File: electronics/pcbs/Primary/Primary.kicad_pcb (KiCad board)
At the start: 2 copper layers, 102 x 53.3 mm, 27 parts, among them J1 Line Sensor 1, J11 I2C Bus, J12 Battery, J13 Pololu_D24V50F5, J14 Magnet, J2 Line Sensor 2, J3 Line Sensor 3, J4 Line Sensor 4, J5 Line Sensor 5, J6 Line Sensor 6, J7 Servo, J8 Pololu_DRV8834, J9 Stepper Motor, P1 Digital, P10 CONN_01X01, P11 CONN_01X01, P12 CONN_01X01, P13 CONN_01X01, P2 Power, P3 Analog, P4 Analog, P5 PWM, P6 PWM, P7 Communication, P8 CONN_01X01, P9 CONN_01X01

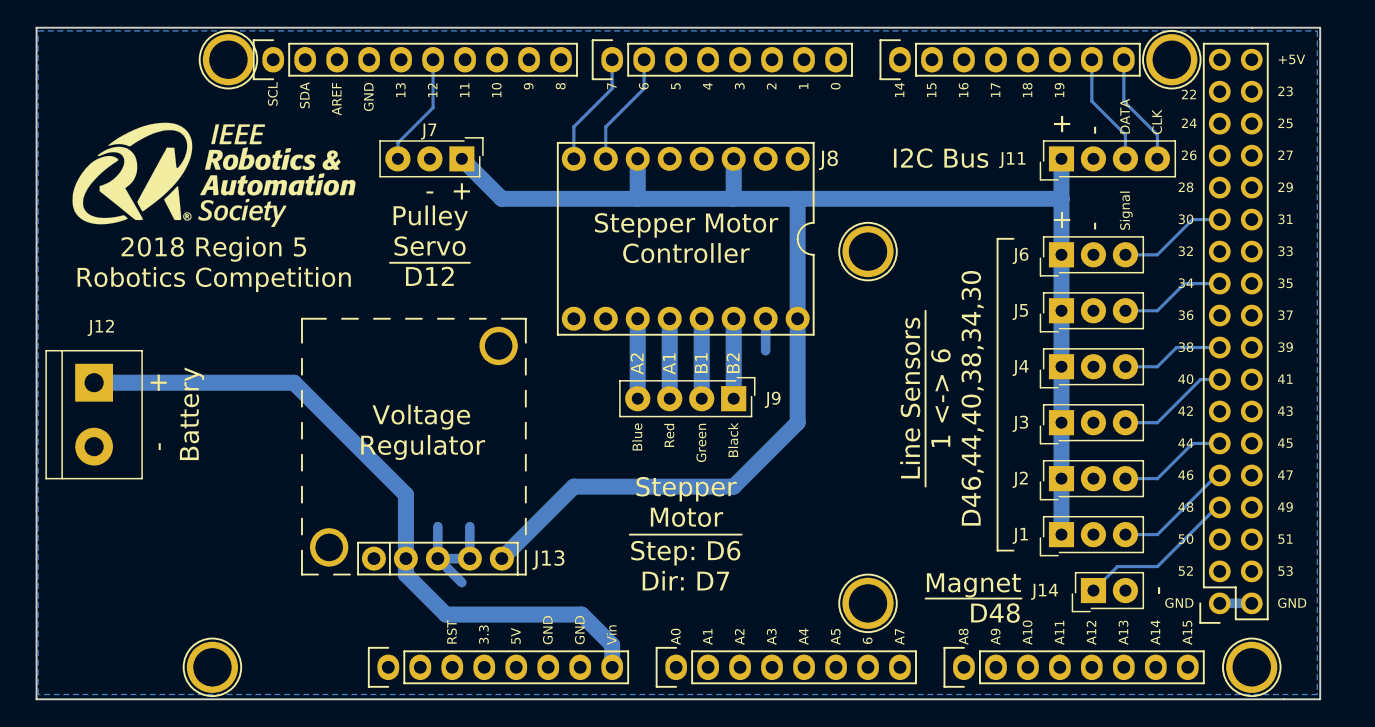
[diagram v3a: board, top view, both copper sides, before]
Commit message: Primary PCB: Modified Primary to be more easily printed with labels on the OtherMill.
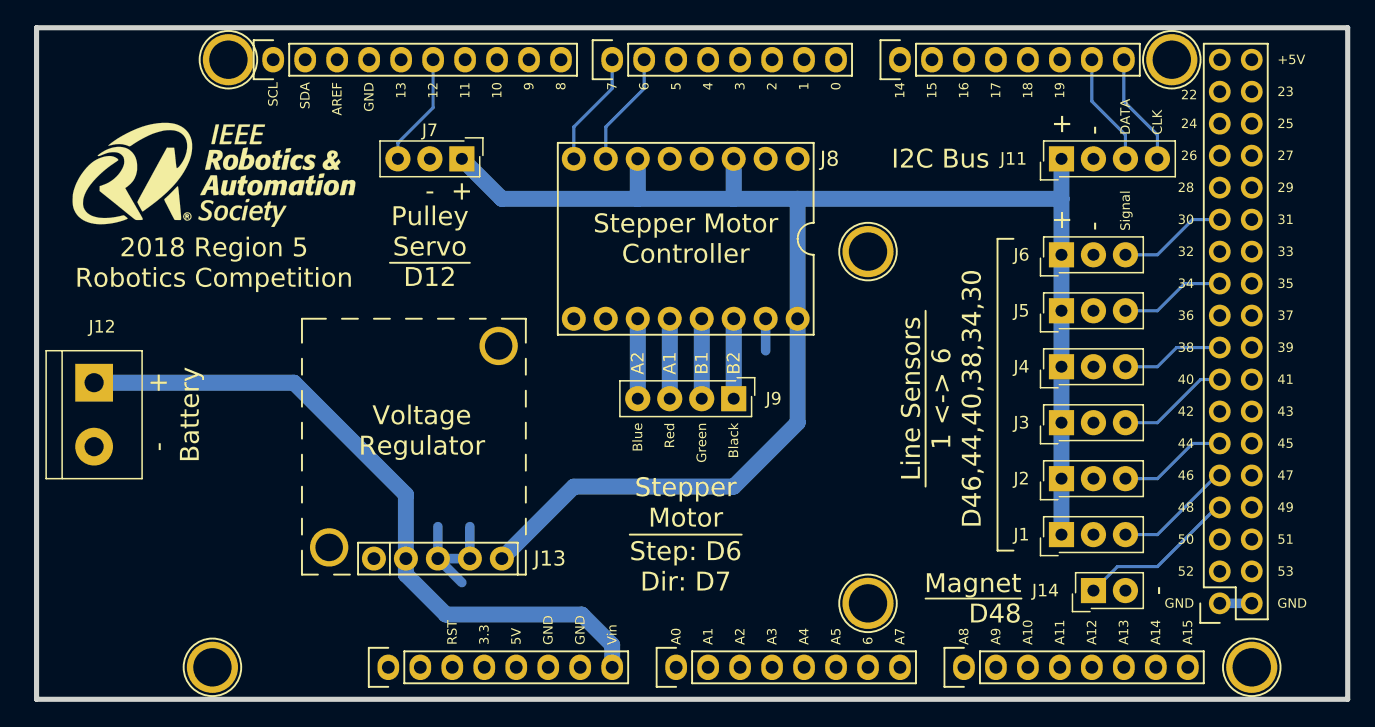
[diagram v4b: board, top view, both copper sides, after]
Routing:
- added copper zone on F.Cu, net GND
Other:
- board size 102 x 53.3 mm -> 104.1 x 53.3 mm
- board text added: "Bk"
- board text added: "Bl"
- board text added: "C"
- board text added: "D"
- board text added: "G"
- board text added: "R"
- board text added: "Sig"
- board text added: "Stepper Motor Step: D6 Dir: D7"

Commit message: Primary PCB: Modified electromagnet circuit to power the magnet with a transistor.
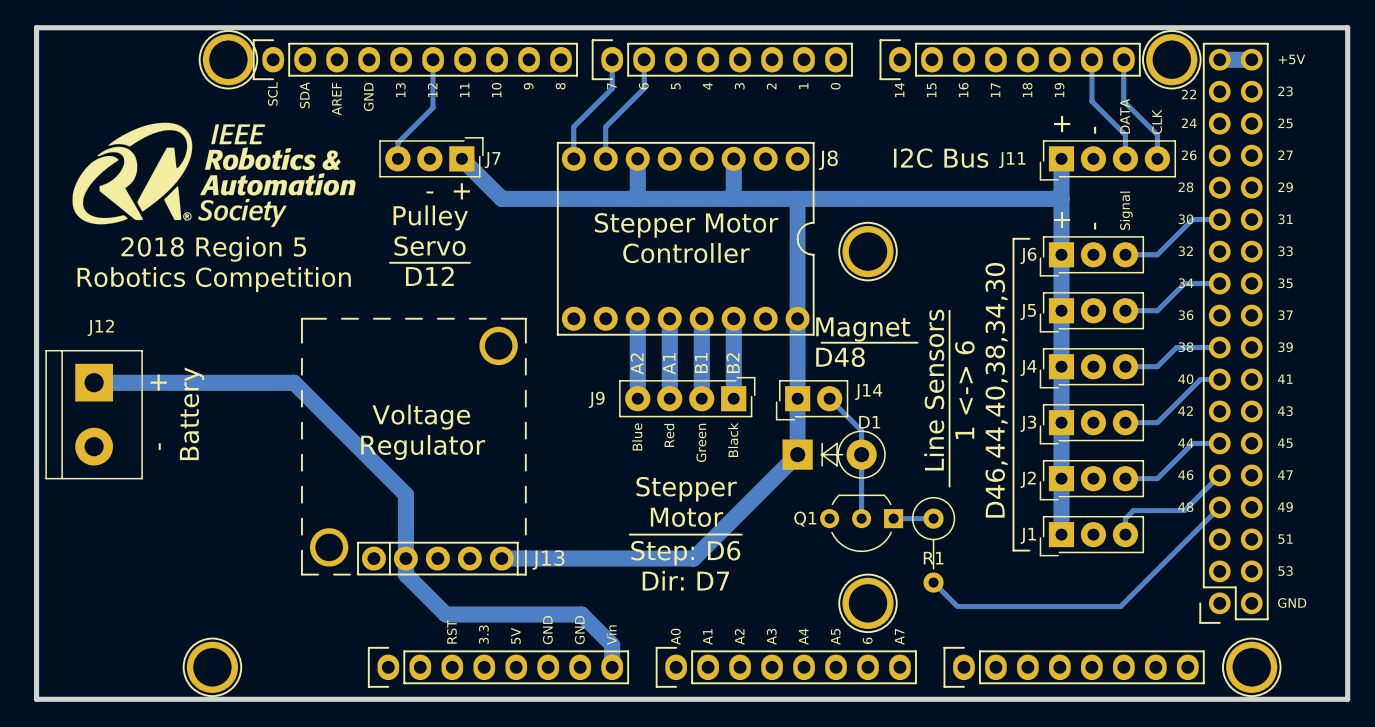
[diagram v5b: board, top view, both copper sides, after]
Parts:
- added D1: D, Diodes_THT:D_DO-15_P5.08mm_Vertical_KathodeUp, F.Cu at (163.8, 102.2)
- added Q1: Q_NPN_BCE, TO_SOT_Packages_THT:TO-92_Inline_Wide, F.Cu at (171.4, 107.3)
- added R1: R, Resistors_THT:R_Axial_DIN0309_L9.0mm_D3.2mm_P5.08mm_Vertical, F.Cu at (174.6, 107.3)
- moved J14 28.0 mm to (163.8, 97.8)
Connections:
- J14 pad 1: /48 -> +5V
- J14 pad 2: GND -> Net-(D1-Pad2)
- P1 pad 35: +5V -> +5VP
- P1 pad 36: +5V -> +5VP
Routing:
- net GND: track 15.4 -> 0.00 mm
- net /48: track 12.8 -> 26.8 mm
- net Net-(D1-Pad2): track 0.00 -> 10.6 mm
- net Net-(Q1-Pad1): track 0.00 -> 3.18 mm
- net +5VP: track 0.00 -> 2.54 mm
- net +5V: track 132.2 -> 133.6 mm
- net /46: track 9.44 -> 10.2 mm
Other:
- net class Default: trace_width 0.25 -> 0.4; via_dia 0.6 -> 0.96; via_drill 0.4 -> 0.64
- net class Ground: clearance 0.2 -> 0.3
- net class HighPower: clearance 0.2 -> 0.3
- board text removed: "50"
- board text removed: "52"
- board text removed: "A10"
- board text removed: "A11"
- board text removed: "A12"
- board text removed: "A13"
- board text removed: "A14"
- board text removed: "A15"
- board text removed: "A8"
- board text removed: "A9"

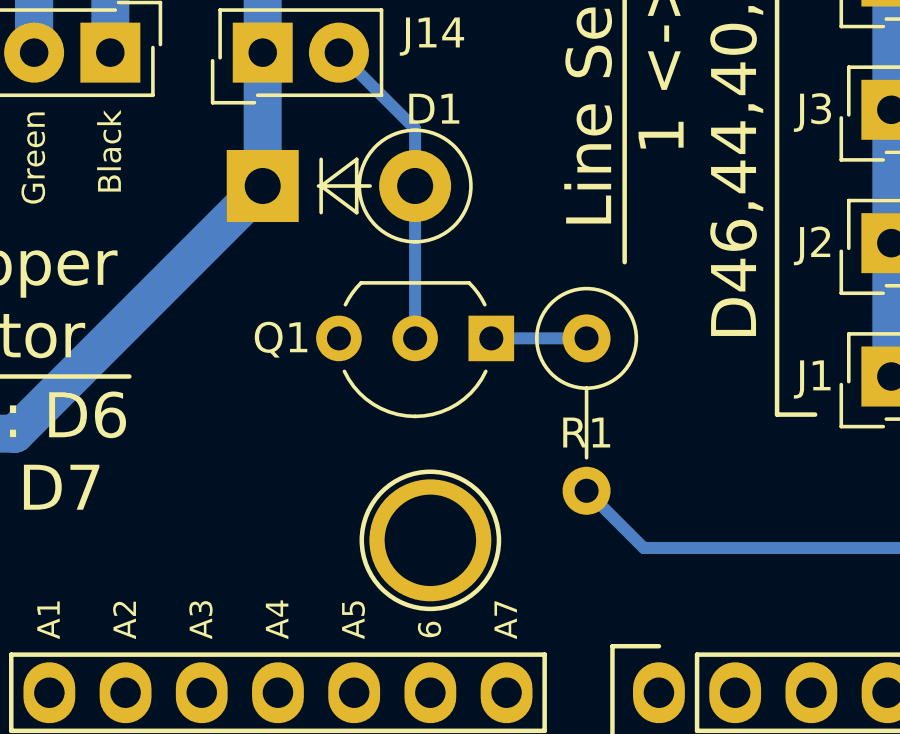
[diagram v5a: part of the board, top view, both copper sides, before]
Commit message: Primary PCB: Corrected transistor pinout and footprint. Gave a value to the resistor attached to the transistor.
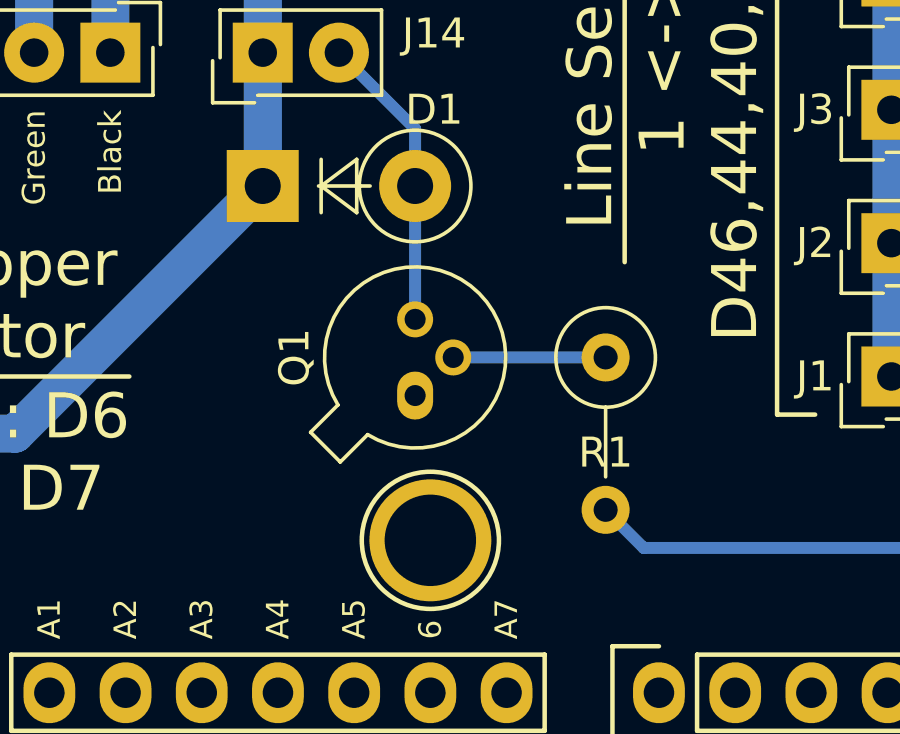
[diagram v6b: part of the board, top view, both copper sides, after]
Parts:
- D1: value D -> 1N914
- Q1: footprint TO_SOT_Packages_THT:TO-92_Inline_Wide -> TO_SOT_Packages_THT:TO-18-3
- R1: value R -> 220
- moved Q1 3.17 mm to (168.9, 109.2), turned to 90 degrees
- moved R1 0.90 mm to (175.3, 108.0)
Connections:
- J13 pad : GND -> (no net)
- Q1 pad 1: Net-(Q1-Pad1) -> GND
- Q1 pad 2: Net-(D1-Pad2) -> Net-(Q1-Pad2)
- Q1 pad 3: GND -> Net-(D1-Pad2)
- R1 pad 1: Net-(Q1-Pad1) -> Net-(Q1-Pad2)
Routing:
- net Net-(Q1-Pad2): track 0.00 -> 5.08 mm
- net Net-(Q1-Pad1): track 3.18 -> 0.00 mm
- net /48: track 26.8 -> 25.9 mm
- net Net-(D1-Pad2): track 10.6 -> 9.94 mm
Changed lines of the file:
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@@
 (kicad_pcb (version 4) (host pcbnew 4.0.7)
   (general
-    (links 62)
+    (links 60)
     (no_connects 1)
     (area 96.952999 66.743 207.721201 123.095)
@@
   (net 90 /A+)
   (net 91 +5VP)
-  (net 92 "Net-(Q1-Pad1)")
-  (net 93 "Net-(D1-Pad2)")
+  (net 92 "Net-(D1-Pad2)")
+  (net 93 "Net-(Q1-Pad2)")
   (net_class Default "This is the default net class."
     (clearance 0.2)
@@
     (add_net "Net-(J8-Pad5)")
     (add_net "Net-(P2-Pad1)")
-    (add_net "Net-(Q1-Pad1)")
+    (add_net "Net-(Q1-Pad2)")
   )
   (net_class Ground ""
@@
       (net 34 +5V))
     (pad 2 thru_hole circle (at 0 2.54 90) (size 2 2) (drill 0.95) (layers *.Cu *.Mask)
-      (net 93 "Net-(D1-Pad2)"))
+      (net 92 "Net-(D1-Pad2)"))
     (model ${KISYS3DMOD}/Connectors_Samtec.3dshapes/SL-102-X-XX_1x02.wrl
       (at (xyz 0 0 0))
@@
     (pad 5 thru_hole circle (at 10.16 0) (size 1.905 1.905) (drill 1.016) (layers *.Cu *.Mask)
       (net 34 +5V))
-    (pad "" thru_hole circle (at -3.556 -0.889) (size 3.048 3.048) (drill 2.1844) (layers *.Cu *.Mask)
-      (net 1 GND))
-    (pad "" thru_hole circle (at 9.906 -16.891) (size 3.048 3.048) (drill 2.1844) (layers *.Cu *.Mask)
-      (net 1 GND))
+    (pad "" thru_hole circle (at -3.556 -0.889) (size 3.048 3.048) (drill 2.1844) (layers *.Cu *.Mask))
+    (pad "" thru_hole circle (at 9.906 -16.891) (size 3.048 3.048) (drill 2.1844) (layers *.Cu *.Mask))
   )
   (module RAS:Logo (layer F.Cu)
@@
   )
   (module Resistors_THT:R_Axial_DIN0309_L9.0mm_D3.2mm_P5.08mm_Vertical (layer F.Cu)
-    (at 174.625 107.315 270)
+    (at 175.26 107.95 270)
     (descr "Resistor, Axial_DIN0309 series, Axial, Vertical, pin pitch=5.08mm, 0.5W = 1/2W, length*diameter=9*3.2mm^2, http://cdn-reichelt.de/documents/datenblatt/B400/1_4W%23YAG.pdf")
     (tags "Resistor Axial_DIN0309 series Axial Vertical pin pitch 5.08mm 0.5W = 1/2W length 9mm diameter 3.2mm")
@@
       (effects (font (size 1 1) (thickness 0.15)))
     )
-    (fp_text value R (at 2.54 2.66 270) (layer F.Fab)
+    (fp_text value 220 (at 2.54 2.66 270) (layer F.Fab)
       (effects (font (size 1 1) (thickness 0.15)))
     )
@@
     (fp_line (start 6.2 -1.95) (end -1.95 -1.95) (layer F.CrtYd) (width 0.05))
     (pad 1 thru_hole circle (at 0 0 270) (size 1.6 1.6) (drill 0.8) (layers *.Cu *.Mask)
-      (net 92 "Net-(Q1-Pad1)"))
+      (net 93 "Net-(Q1-Pad2)"))
     (pad 2 thru_hole oval (at 5.08 0 270) (size 1.6 1.6) (drill 0.8) (layers *.Cu *.Mask)
       (net 6 /48))
@@
       (effects (font (size 1 1) (thickness 0.15)))
     )
-    (fp_text value D (at 2.54 2.86) (layer F.Fab)
+    (fp_text value 1N914 (at 2.54 2.86) (layer F.Fab)
       (effects (font (size 1 1) (thickness 0.15)))
     )
@@
       (net 34 +5V))
     (pad 2 thru_hole oval (at 5.08 0) (size 2.4 2.4) (drill 1.2) (layers *.Cu *.Mask)
-      (net 93 "Net-(D1-Pad2)"))
+      (net 92 "Net-(D1-Pad2)"))
     (model ${KISYS3DMOD}/Diodes_THT.3dshapes/D_DO-15_P5.08mm_Vertical_KathodeUp.wrl
       (at (xyz 0 0 0))
@@
     )
   )
-  (module TO_SOT_Packages_THT:TO-92_Inline_Wide (layer F.Cu)
-    (at 171.45 107.315 180)
-    (descr "TO-92 leads in-line, wide, drill 0.8mm (see NXP sot054_po.pdf)")
-    (tags "to-92 sc-43 sc-43a sot54 PA33 transistor")
-    (fp_text reference Q1 (at 6.985 0 360) (layer F.SilkS)
-      (effects (font (size 1 1) (thickness 0.15)))
-    )
-    (fp_text value Q_NPN_BCE (at 2.54 2.79 180) (layer F.Fab)
-      (effects (font (size 1 1) (thickness 0.15)))
-    )
-    (fp_text user %R (at 2.54 -3.56 360) (layer F.Fab)
-      (effects (font (size 1 1) (thickness 0.15)))
-    )
-    (fp_line (start 0.74 1.85) (end 4.34 1.85) (layer F.SilkS) (width 0.12))
-    (fp_line (start 0.8 1.75) (end 4.3 1.75) (layer F.Fab) (width 0.1))
-    (fp_line (start -1.01 -2.73) (end 6.09 -2.73) (layer F.CrtYd) (width 0.05))
-    (fp_line (start -1.01 -2.73) (end -1.01 2.01) (layer F.CrtYd) (width 0.05))
-    (fp_line (start 6.09 2.01) (end 6.09 -2.73) (layer F.CrtYd) (width 0.05))
-    (fp_line (start 6.09 2.01) (end -1.01 2.01) (layer F.CrtYd) (width 0.05))
-    (fp_arc (start 2.54 0) (end 0.74 1.85) (angle 20) (layer F.SilkS) (width 0.12))
-    (fp_arc (start 2.54 0) (end 2.54 -2.6) (angle -65) (layer F.SilkS) (width 0.12))
-    (fp_arc (start 2.54 0) (end 2.54 -2.6) (angle 65) (layer F.SilkS) (width 0.12))
-    (fp_arc (start 2.54 0) (end 2.54 -2.48) (angle 135) (layer F.Fab) (width 0.1))
-    (fp_arc (start 2.54 0) (end 2.54 -2.48) (angle -135) (layer F.Fab) (width 0.1))
-    (fp_arc (start 2.54 0) (end 4.34 1.85) (angle -20) (layer F.SilkS) (width 0.12))
-    (pad 2 thru_hole circle (at 2.54 0 270) (size 1.52 1.52) (drill 0.8) (layers *.Cu *.Mask)
-      (net 93 "Net-(D1-Pad2)"))
-    (pad 3 thru_hole circle (at 5.08 0 270) (size 1.52 1.52) (drill 0.8) (layers *.Cu *.Mask)
-      (net 1 GND))
-    (pad 1 thru_hole rect (at 0 0 270) (size 1.52 1.52) (drill 0.8) (layers *.Cu *.Mask)
-      (net 92 "Net-(Q1-Pad1)"))
-    (model ${KISYS3DMOD}/TO_SOT_Packages_THT.3dshapes/TO-92_Inline_Wide.wrl
-      (at (xyz 0.1 0 0))
-      (scale (xyz 1 1 1))
-      (rotate (xyz 0 0 -90))
+  (module TO_SOT_Packages_THT:TO-18-3 (layer F.Cu)
+    (at 168.91 109.22 90)
+    (descr TO-18-3)
+    (tags TO-18-3)
+    (fp_text reference Q1 (at 1.27 -4.02 90) (layer F.SilkS)
+      (effects (font (size 1 1) (thickness 0.15)))
+    )
+    (fp_text value Q_NPN_BCE (at 1.27 4.02 90) (layer F.Fab)
+      (effects (font (size 1 1) (thickness 0.15)))
+    )
+    (fp_text user %R (at 1.27 -4.02 90) (layer F.Fab)
+      (effects (font (size 1 1) (thickness 0.15)))
+    )
+    (fp_line (start -0.329057 -2.419301) (end -1.156372 -3.246616) (layer F.Fab) (width 0.1))
+    (fp_line (start -1.156372 -3.246616) (end -1.976616 -2.426372) (layer F.Fab) (width 0.1))
+    (fp_line (start -1.976616 -2.426372) (end -1.149301 -1.599057) (layer F.Fab) (width 0.1))
+    (fp_line (start -0.312331 -2.572281) (end -1.224499 -3.484448) (layer F.SilkS) (width 0.12))
+    (fp_line (start -1.224499 -3.484448) (end -2.214448 -2.494499) (layer F.SilkS) (width 0.12))
+    (fp_line (start -2.214448 -2.494499) (end -1.302281 -1.582331) (layer F.SilkS) (width 0.12))
+    (fp_line (start -2.23 -3.5) (end -2.23 3.15) (layer F.CrtYd) (width 0.05))
+    (fp_line (start -2.23 3.15) (end 4.42 3.15) (layer F.CrtYd) (width 0.05))
+    (fp_line (start 4.42 3.15) (end 4.42 -3.5) (layer F.CrtYd) (width 0.05))
+    (fp_line (start 4.42 -3.5) (end -2.23 -3.5) (layer F.CrtYd) (width 0.05))
+    (fp_circle (center 1.27 0) (end 3.67 0) (layer F.Fab) (width 0.1))
+    (fp_arc (start 1.27 0) (end -0.329057 -2.419301) (angle 336.9) (layer F.Fab) (width 0.1))
+    (fp_arc (start 1.27 0) (end -0.312331 -2.572281) (angle 333.2) (layer F.SilkS) (width 0.12))
+    (pad 1 thru_hole oval (at 0 0 90) (size 1.6 1.2) (drill 0.7) (layers *.Cu *.Mask)
+      (net 1 GND))
+    (pad 2 thru_hole oval (at 1.27 1.27 90) (size 1.2 1.2) (drill 0.7) (layers *.Cu *.Mask)
+      (net 93 "Net-(Q1-Pad2)"))
+    (pad 3 thru_hole oval (at 2.54 0 90) (size 1.2 1.2) (drill 0.7) (layers *.Cu *.Mask)
+      (net 92 "Net-(D1-Pad2)"))
+    (model ${KISYS3DMOD}/TO_SOT_Packages_THT.3dshapes/TO-18-3.wrl
+      (at (xyz 0 0 0))
+      (scale (xyz 0.393701 0.393701 0.393701))
+      (rotate (xyz 0 0 0))
     )
   )
@@
   (gr_line (start 103.378 68.326) (end 207.518 68.326) (angle 90) (layer Edge.Cuts) (width 0.4064))
   (gr_line (start 103.378 121.666) (end 103.378 68.326) (angle 90) (layer Edge.Cuts) (width 0.4064))
-  (segment (start 174.625 112.395) (end 176.53 114.3) (width 0.4) (layer B.Cu) (net 6))
-  (segment (start 189.484 114.3) (end 197.358 106.426) (width 0.4) (layer B.Cu) (net 6))
+  (segment (start 175.26 113.03) (end 176.53 114.3) (width 0.4) (layer B.Cu) (net 6))
   (segment (start 176.53 114.3) (end 189.484 114.3) (width 0.4) (layer B.Cu) (net 6))
+  (segment (start 189.484 114.3) (end 197.358 106.426) (width 0.4) (layer B.Cu) (net 6))
   (segment (start 189.865 108.585) (end 189.865 107.315) (width 0.4) (layer B.Cu) (net 8))
   (segment (start 194.564 106.68) (end 197.358 103.886) (width 0.4) (layer B.Cu) (net 8))
@@
   (segment (start 151.13 91.44) (end 151.13 97.79) (width 1.27) (layer B.Cu) (net 90))
   (segment (start 197.358 70.866) (end 199.898 70.866) (width 1.27) (layer B.Cu) (net 91))
-  (segment (start 171.45 107.315) (end 174.625 107.315) (width 0.4) (layer B.Cu) (net 92) (status 10))
-  (segment (start 168.91 107.315) (end 168.91 102.235) (width 0.4) (layer B.Cu) (net 93))
-  (segment (start 168.91 102.235) (end 168.91 100.33) (width 0.4) (layer B.Cu) (net 93))
-  (segment (start 168.91 100.33) (end 166.37 97.79) (width 0.4) (layer B.Cu) (net 93))
+  (segment (start 168.91 106.68) (end 168.91 102.235) (width 0.4) (layer B.Cu) (net 92))
+  (segment (start 168.91 102.235) (end 168.91 100.33) (width 0.4) (layer B.Cu) (net 92))
+  (segment (start 168.91 100.33) (end 166.37 97.79) (width 0.4) (layer B.Cu) (net 92))
+  (segment (start 170.18 107.95) (end 175.26 107.95) (width 0.4) (layer B.Cu) (net 93))
   (zone (net 1) (net_name GND) (layer B.Cu) (hatch edge 0.508)
     (connect_pads (clearance 0.508))
